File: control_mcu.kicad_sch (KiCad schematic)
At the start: 18 parts, among them J601 Conn_02x07_Counter_Clockwise, J602 Conn_01x02, U601 ATtiny1614-SSNR, U602 RCLAMP0524P-N

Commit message: SH-RPi v2 schematic design
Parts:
- removed D602, D603: MSK4005, Diode_SMD:D_SOD-523, symbol Device:D_Schottky
- removed J601: Conn_02x07_Counter_Clockwise, SH-RPi:PinHeader_2x07_P2.54mm_Vertical_CounterClockwise, symbol Connector_Generic:Conn_02x07_Counter_Clockwise
- removed U601: ATtiny1614-SSNR, Package_SO:SOIC-14_3.9x8.7mm_P1.27mm, symbol MCU_Microchip_ATtiny:ATtiny1614-SS
- removed U602: RCLAMP0524P-N, Package_DFN_QFN:Diodes_UDFN-10_1.0x2.5mm_P0.5mm, symbol SH-RPi:RCLAMP0524P-N
- added C402: 33pF/50V, Capacitor_SMD:C_0603_1608Metric, symbol Device:C
- added C405: 33pF, Capacitor_SMD:C_0402_1005Metric, symbol Device:C
- added D401, D402: ESD5451N, Diode_SMD:D_0402_1005Metric, symbol Device:D_TVS
- added FB402: GZ2012D101TF, Inductor_SMD:L_0805_2012Metric, symbol Device:FerriteBead
- added J402: Conn_01x02, Connector_PinHeader_2.54mm:PinHeader_1x02_P2.54mm_Vertical, symbol Connector_Generic:Conn_01x02
- added J403: Conn_02x06_Odd_Even, symbol Connector_Generic:Conn_02x06_Odd_Even
- added R406: 100R, Resistor_SMD:R_0603_1608Metric, symbol Device:R
- added R408: 1k, symbol Device:R_Small
- added R409: 10k, Resistor_SMD:R_0402_1005Metric, symbol Device:R
- added R410: 100k, Resistor_SMD:R_0402_1005Metric, symbol Device:R
- added U401: ATtiny1616-M, Package_DFN_QFN:VQFN-20-1EP_3x3mm_P0.4mm_EP1.7x1.7mm, symbol MCU_Microchip_ATtiny:ATtiny1616-M
- R402: renamed from R604; value 300k -> 150k; LCSC C25774 -> (none)
- R403: renamed from R605; value 200k -> 20k; LCSC C25764 -> (none)
- renumbered C603 to C401, C601 to C403, C604 to C404, C602 to C406, D601 to D403, FB601 to FB401, J602 to J401, R601 to R401, R602 to R404, R606 to R405, R603 to R407
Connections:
- net ATT_Vcc is gone; now on net +3V3: C406.1, D403.1 (K), R407.1
- net +3V3: now also J403.6 (Pin_6), U401.4 (VCC)
- net EN5V: now also R409.2, R410.1
- net GND: now also C402.2, C405.2, D401.1 (A1), D402.1 (A1), J402.2 (Pin_2), J403.7 (Pin_7), J403.8 (Pin_8), R410.2, U401.21 (GND), U401.3 (GND)
- net RESET: now also J403.3 (Pin_3), R408.2, U401.19 (~{RESET}/PA0)
- net RXD: now also J403.9 (Pin_9), U401.11 (PB3)
- net SCL: now also U401.14 (PB0)
- net SDA: now also U401.13 (PB1)
- net TXD: now also J403.11 (Pin_11), U401.12 (PB2)
- net VcapS: now also U401.8 (PA7)
- net VinS: now also U401.7 (PA6)
- net EXT_INT renamed EXT
- net EXT: now also U401.16 (PC1)
- net PB0_CONN renamed EXT_CONN
- net EXT_CONN: now also D401.2 (A2)
- new net: J403.1 (Pin_1), R408.1
- new net: C405.1, FB402.1, R406.2
- new net EN5V_MCU: R409.1, U401.18 (PC3)
- new net EN_OUT: J403.5 (Pin_5)
- new net Iin: U401.10 (PB4)
- new net LED_1: U401.1 (PA2)
- new net LED_2: U401.2 (PA3)
- new net LED_3: U401.5 (PA4)
- new net LED_4: U401.6 (PA5)
- new net POWER_TOGGLE: R406.1, U401.15 (PC0)
- new net POW_CONN: C402.1, D402.2 (A2), FB402.2, J402.1 (Pin_1)
- new net RTC_INT: U401.17 (PC2)
- new net RXD0: J403.12 (Pin_12)
- new net RXD5: J403.4 (Pin_4)
- new net TXD0: J403.10 (Pin_10)
- new net TXD5: J403.2 (Pin_2)
- no-connect marks 4 -> 2
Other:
- note added: "5V output enable interface"
- note added: "Clamp VinS to always less than 3V3"
- note added: "ESD and EMI protection for external connectors"
- note added: "Programming connector"
- note added: "Resistor pulls EN down when the MCU is unpowered"
- note added: "Scale Vcap down to ADC input"
- note added: "Scale Vin down to ADC input"
- note added: "VcapS is scaled from 9.35V to 1.1V (this will also drain the cap over time)"
- note removed: "Clamp VinS to always less than ATT_Vcc"
- note removed: "VcapS is scaled from 2.75V to 1.1V (this will also drain the cap over time)"
- moved on the sheet: C401, C403, C404, C406, D403, FB401, J401, R401, R402, R403, R404, R405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

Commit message: WIP: Assign footprints and LCSC part numbers
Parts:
- J403: footprint (none) -> Connector_PinHeader_2.54mm:PinHeader_2x06_P2.54mm_Vertical; LCSC (none) -> C492423
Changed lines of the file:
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@@
     (property "Reference" "J403" (id 0) (at 245.11 63.5 0))
     (property "Value" "Conn_02x06_Odd_Even" (id 1) (at 245.11 66.04 0))
-    (property "Footprint" "" (id 2) (at 243.84 74.93 0)
+    (property "Footprint" "Connector_PinHeader_2.54mm:PinHeader_2x06_P2.54mm_Vertical" (id 2) (at 243.84 74.93 0)
       (effects (font (size 1.27 1.27)) hide)
     )
@@
       (effects (font (size 1.27 1.27)) hide)
     )
+    (property "LCSC" "C492423" (id 4) (at 243.84 74.93 0)
+      (effects (font (size 1.27 1.27)) hide)
+    )

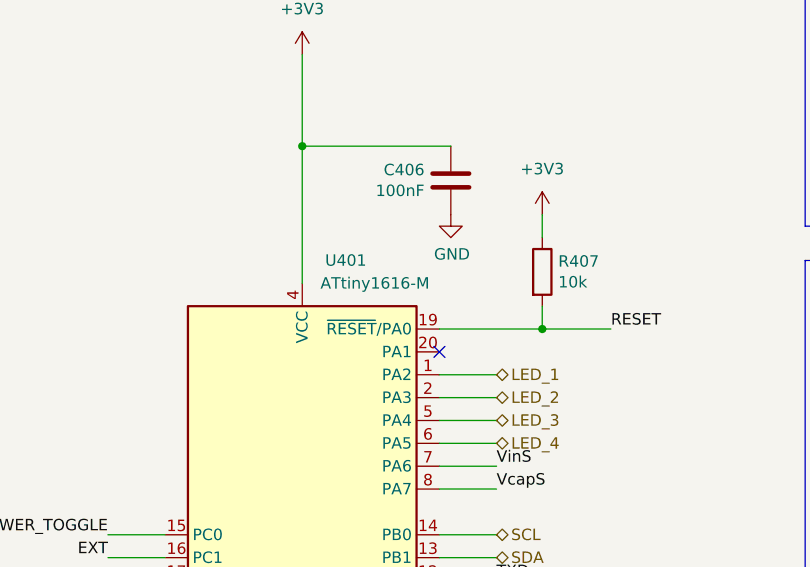
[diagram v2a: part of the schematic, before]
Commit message: Assign footprints and part numbers to components
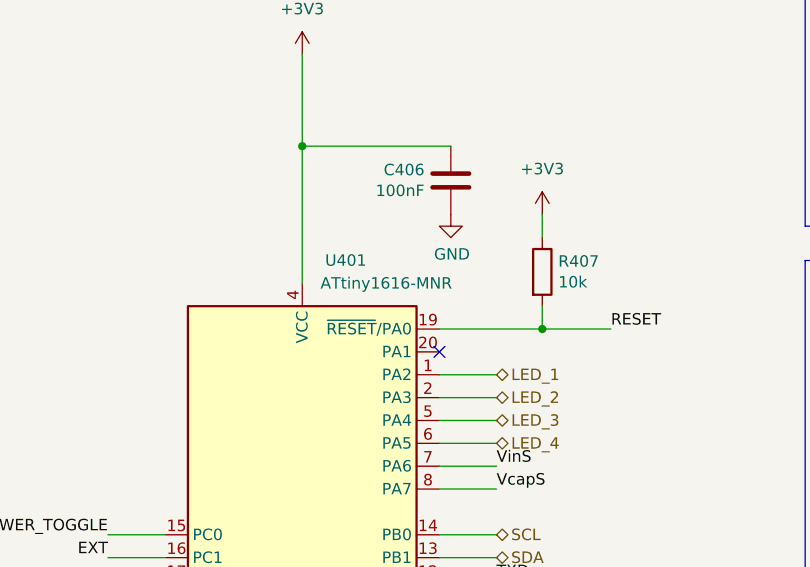
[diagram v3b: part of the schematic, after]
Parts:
- R402: LCSC (none) -> C25755
- R403: LCSC (none) -> C25765
- R408: footprint (none) -> Resistor_SMD:R_0402_1005Metric; LCSC (none) -> C11702
- U401: value ATtiny1616-M -> ATtiny1616-MNR; LCSC (none) -> C507118
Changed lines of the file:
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@@
       (effects (font (size 1.27 1.27)) hide)
     )
-    (property "LCSC" "" (id 4) (at 71.12 176.53 0)
+    (property "LCSC" "C25765" (id 4) (at 71.12 176.53 0)
       (effects (font (size 1.27 1.27)) hide)
     )
@@
       (effects (font (size 1.27 1.27)) hide)
     )
-    (property "LCSC" "" (id 4) (at 71.12 163.83 0)
+    (property "LCSC" "C25755" (id 4) (at 71.12 163.83 0)
       (effects (font (size 1.27 1.27)) hide)
     )
@@
       (effects (font (size 1.27 1.27)) (justify left))
     )
-    (property "Footprint" "" (id 2) (at 217.17 71.12 0)
+    (property "Footprint" "Resistor_SMD:R_0402_1005Metric" (id 2) (at 217.17 71.12 0)
       (effects (font (size 1.27 1.27)) hide)
     )
@@
       (effects (font (size 1.27 1.27)) hide)
     )
+    (property "LCSC" "C11702" (id 4) (at 217.17 71.12 0)
+      (effects (font (size 1.27 1.27)) hide)
+    )
     (pin "1")
     (pin "2")
@@
       (effects (font (size 1.27 1.27)) (justify left))
     )
-    (property "Value" "ATtiny1616-M" (id 1) (at 150.6094 55.88 0)
+    (property "Value" "ATtiny1616-MNR" (id 1) (at 150.6094 55.88 0)
       (effects (font (size 1.27 1.27)) (justify left))
     )
@@
       (effects (font (size 1.27 1.27)) hide)
     )
+    (property "LCSC" "C507118" (id 4) (at 148.59 78.74 0)
+      (effects (font (size 1.27 1.27)) hide)
+    )

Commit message: WIP: PCB layout
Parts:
- removed J401, J402: Conn_01x02, Connector_PinHeader_2.54mm:PinHeader_1x02_P2.54mm_Vertical, symbol Connector_Generic:Conn_01x02
- added J401: Conn_02x02_Top_Bottom, Connector_PinHeader_2.54mm:PinHeader_2x02_P2.54mm_Vertical, symbol Connector_Generic:Conn_02x02_Top_Bottom
- R401: value 62k -> 56k; footprint Resistor_SMD:R_0603_1608Metric -> Resistor_SMD:R_0402_1005Metric; LCSC C23221 -> C25796
- R404: value 2.2k -> 2k; LCSC C25879 -> C4109
- R405, R406: footprint Resistor_SMD:R_0603_1608Metric -> Resistor_SMD:R_0402_1005Metric; LCSC C22775 -> C25076
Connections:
- net EXT_CONN: now also J401.4 (Pin_4)
- net GND: now also J401.1 (Pin_1), J401.3 (Pin_3)
- net POW_CONN: now also J401.2 (Pin_2)
- net TXD5J: now reaches J403.1 (Pin_1), R408.1
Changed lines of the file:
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@@
     (stroke (width 0) (type default) (color 0 0 0 0))
   )
-  (wire (pts (xy 26.67 33.02) (xy 31.75 33.02))
+  (wire (pts (xy 19.05 33.02) (xy 31.75 33.02))
     (stroke (width 0) (type default) (color 0 0 0 0))
   )
@@
     (stroke (width 0) (type default) (color 0 0 0 0))
   )
-  (wire (pts (xy 26.67 30.48) (xy 39.37 30.48))
+  (wire (pts (xy 21.59 30.48) (xy 39.37 30.48))
     (stroke (width 0) (type default) (color 0 0 0 0))
   )
@@
     (stroke (width 0) (type default) (color 0 0 0 0))
   )
+  (wire (pts (xy 19.05 33.02) (xy 19.05 40.64))
+    (stroke (width 0) (type default) (color 0 0 0 0))
+  )
   (wire (pts (xy 163.83 76.2) (xy 170.18 76.2))
     (stroke (width 0) (type default) (color 0 0 0 0))
@@
     (stroke (width 0) (type default) (color 0 0 0 0))
   )
+  (wire (pts (xy 19.05 63.5) (xy 19.05 53.34))
+    (stroke (width 0) (type default) (color 0 0 0 0))
+  )
   (wire (pts (xy 251.46 74.93) (xy 262.89 74.93))
     (stroke (width 0) (type default) (color 0 0 0 0))
@@
     (stroke (width 0) (type default) (color 0 0 0 0))
   )
+  (wire (pts (xy 21.59 30.48) (xy 21.59 40.64))
+    (stroke (width 0) (type default) (color 0 0 0 0))
+  )
   (wire (pts (xy 41.91 118.11) (xy 64.77 118.11))
     (stroke (width 0) (type default) (color 0 0 0 0))
@@
     (stroke (width 0) (type default) (color 0 0 0 0))
   )
-  (wire (pts (xy 26.67 60.96) (xy 39.37 60.96))
+  (wire (pts (xy 21.59 60.96) (xy 39.37 60.96))
     (stroke (width 0) (type default) (color 0 0 0 0))
   )
@@
     (stroke (width 0) (type default) (color 0 0 0 0))
   )
+  (wire (pts (xy 21.59 60.96) (xy 21.59 53.34))
+    (stroke (width 0) (type default) (color 0 0 0 0))
+  )
   (polyline (pts (xy 269.24 53.34) (xy 269.24 87.63))
     (stroke (width 0) (type default) (color 0 0 0 0))
@@
     (stroke (width 0) (type default) (color 0 0 0 0))
   )
-  (wire (pts (xy 26.67 63.5) (xy 31.75 63.5))
+  (wire (pts (xy 19.05 63.5) (xy 31.75 63.5))
     (stroke (width 0) (type default) (color 0 0 0 0))
   )
@@
     (effects (font (size 1.27 1.27)) (justify right bottom))
   )
+  (label "TXD5J" (at 236.22 69.85 180)
+    (effects (font (size 1.27 1.27)) (justify right bottom))
+  )
   (label "POW_CONN" (at 44.45 60.96 0)
     (effects (font (size 1.27 1.27)) (justify left bottom))
@@
       (effects (font (size 1.27 1.27)) (justify left))
     )
-    (property "Value" "62k" (id 1) (at 66.548 112.903 0)
-      (effects (font (size 1.27 1.27)) (justify left))
-    )
-    (property "Footprint" "Resistor_SMD:R_0603_1608Metric" (id 2) (at 62.992 111.76 90)
+    (property "Value" "56k" (id 1) (at 66.548 112.903 0)
+      (effects (font (size 1.27 1.27)) (justify left))
+    )
+    (property "Footprint" "Resistor_SMD:R_0402_1005Metric" (id 2) (at 62.992 111.76 90)
       (effects (font (size 1.27 1.27)) hide)
     )
@@
       (effects (font (size 1.27 1.27)) hide)
     )
-    (property "LCSC" "C23221" (id 4) (at 64.77 111.76 0)
+    (property "LCSC" "C25796" (id 4) (at 64.77 111.76 0)
       (effects (font (size 1.27 1.27)) hide)
     )
@@
       (effects (font (size 1.27 1.27)) (justify left))
     )
-    (property "Value" "2.2k" (id 1) (at 81.788 125.603 0)
+    (property "Value" "2k" (id 1) (at 81.788 125.603 0)
       (effects (font (size 1.27 1.27)) (justify left))
     )
@@
       (effects (font (size 1.27 1.27)) hide)
     )
-    (property "LCSC" "C25879" (id 4) (at 80.01 124.46 0)
+    (property "LCSC" "C4109" (id 4) (at 80.01 124.46 0)
       (effects (font (size 1.27 1.27)) hide)
     )
@@
     )
     (property "LCSC" "C25755" (id 4) (at 71.12 163.83 0)
-      (effects (font (size 1.27 1.27)) hide)
-    )
-    (pin "1")
-    (pin "2")
-  )
-  (symbol (lib_id "Connector_Generic:Conn_01x02") (at 21.59 30.48 0) (mirror y) (unit 1)
-    (in_bom yes) (on_board yes)
-    (property "Reference" "J401" (id 0) (at 23.6728 24.9682 0))
-    (property "Value" "Conn_01x02" (id 1) (at 23.6728 27.2796 0))
-    (property "Footprint" "Connector_PinHeader_2.54mm:PinHeader_1x02_P2.54mm_Vertical" (id 2) (at 21.59 30.48 0)
-      (effects (font (size 1.27 1.27)) hide)
-    )
-    (property "Datasheet" "~" (id 3) (at 21.59 30.48 0)
-      (effects (font (size 1.27 1.27)) hide)
-    )
-    (property "LCSC" "C492401" (id 4) (at 21.59 30.48 0)
       (effects (font (size 1.27 1.27)) hide)
     )
@@
     (property "Reference" "R405" (id 0) (at 81.28 25.2222 90))
     (property "Value" "100R" (id 1) (at 81.28 27.5336 90))
-    (property "Footprint" "Resistor_SMD:R_0603_1608Metric" (id 2) (at 81.28 28.702 90)
+    (property "Footprint" "Resistor_SMD:R_0402_1005Metric" (id 2) (at 81.28 28.702 90)
       (effects (font (size 1.27 1.27)) hide)
     )
@@
       (effects (font (size 1.27 1.27)) hide)
     )
-    (property "LCSC" "C22775" (id 4) (at 81.28 30.48 90)
+    (property "LCSC" "C25076" (id 4) (at 81.28 30.48 90)
       (effects (font (size 1.27 1.27)) hide)
     )
@@
     (property "Reference" "R406" (id 0) (at 81.28 55.7022 90))
     (property "Value" "100R" (id 1) (at 81.28 58.0136 90))
-    (property "Footprint" "Resistor_SMD:R_0603_1608Metric" (id 2) (at 81.28 59.182 90)
+    (property "Footprint" "Resistor_SMD:R_0402_1005Metric" (id 2) (at 81.28 59.182 90)
       (effects (font (size 1.27 1.27)) hide)
     )
@@
       (effects (font (size 1.27 1.27)) hide)
     )
-    (property "LCSC" "C22775" (id 4) (at 81.28 60.96 90)
-      (effects (font (size 1.27 1.27)) hide)
-    )
-    (pin "1")
-    (pin "2")
-  )
-  (symbol (lib_id "Connector_Generic:Conn_01x02") (at 21.59 60.96 0) (mirror y) (unit 1)
-    (in_bom yes) (on_board yes)
-    (property "Reference" "J402" (id 0) (at 23.6728 55.4482 0))
-    (property "Value" "Conn_01x02" (id 1) (at 23.6728 57.7596 0))
-    (property "Footprint" "Connector_PinHeader_2.54mm:PinHeader_1x02_P2.54mm_Vertical" (id 2) (at 21.59 60.96 0)
-      (effects (font (size 1.27 1.27)) hide)
-    )
-    (property "Datasheet" "~" (id 3) (at 21.59 60.96 0)
-      (effects (font (size 1.27 1.27)) hide)
-    )
-    (property "LCSC" "C492401" (id 4) (at 21.59 60.96 0)
+    (property "LCSC" "C25076" (id 4) (at 81.28 60.96 90)
       (effects (font (size 1.27 1.27)) hide)
     )
@@
     (pin "1")
   )
+  (symbol (lib_id "Connector_Generic:Conn_02x02_Top_Bottom") (at 19.05 48.26 90) (unit 1)
+    (in_bom yes) (on_board yes)
+    (property "Reference" "J401" (id 0) (at 22.86 52.07 90)
+      (effects (font (size 1.27 1.27)) (justify right))
+    )
+    (property "Value" "Conn_02x02_Top_Bottom" (id 1) (at 22.86 54.61 90)
+      (effects (font (size 1.27 1.27)) (justify right))
+    )
+    (property "Footprint" "Connector_PinHeader_2.54mm:PinHeader_2x02_P2.54mm_Vertical" (id 2) (at 19.05 48.26 0)
+      (effects (font (size 1.27 1.27)) hide)
+    )
+    (property "Datasheet" "~" (id 3) (at 19.05 48.26 0)
+      (effects (font (size 1.27 1.27)) hide)
+    )
+    (pin "1")
+    (pin "2")
+    (pin "3")
+    (pin "4")
+  )
 )

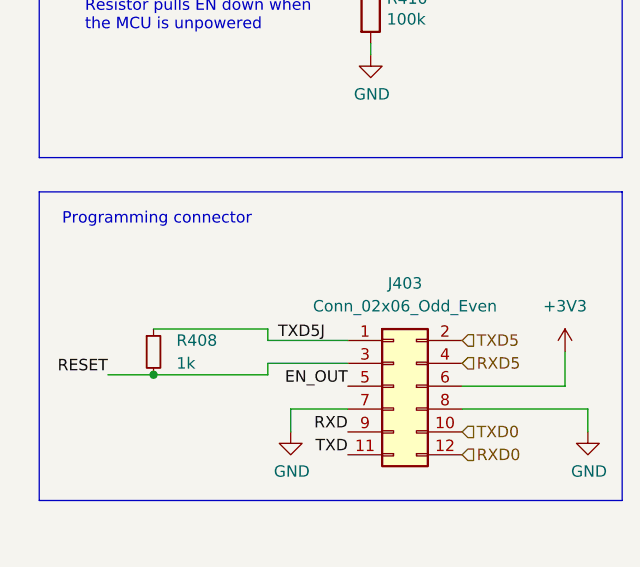
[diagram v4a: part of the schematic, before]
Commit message: Initial PCB component layout done
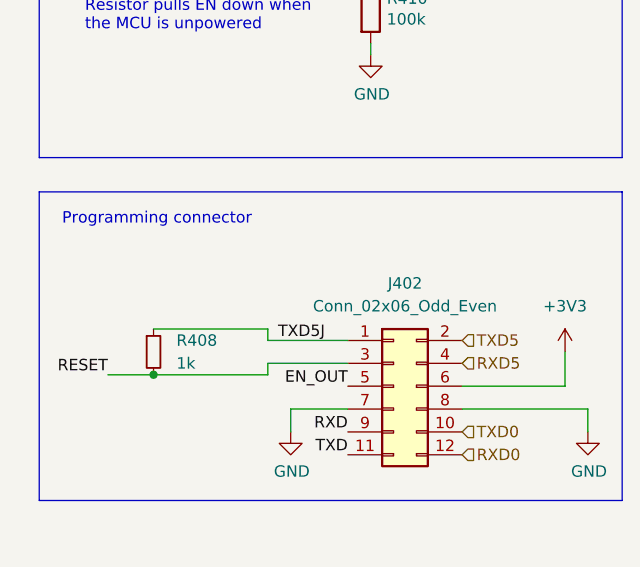
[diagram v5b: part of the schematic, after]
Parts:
- renumbered J403 to J402
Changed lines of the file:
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@@
   (symbol (lib_id "Connector_Generic:Conn_02x06_Odd_Even") (at 243.84 74.93 0) (unit 1)
     (in_bom yes) (on_board yes) (fields_autoplaced)
-    (property "Reference" "J403" (id 0) (at 245.11 63.5 0))
+    (property "Reference" "J402" (id 0) (at 245.11 63.5 0))
     (property "Value" "Conn_02x06_Odd_Even" (id 1) (at 245.11 66.04 0))
     (property "Footprint" "Connector_PinHeader_2.54mm:PinHeader_2x06_P2.54mm_Vertical" (id 2) (at 243.84 74.93 0)

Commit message: Finish PCB routing
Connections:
- net EN_OUT is gone; now on net EN5V: J402.5 (Pin_5)
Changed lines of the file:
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@@
     (effects (font (size 1.27 1.27)) (justify left bottom))
   )
-  (label "EN_OUT" (at 238.76 74.93 180)
+  (label "EN5V" (at 238.76 74.93 180)
     (effects (font (size 1.27 1.27)) (justify right bottom))
   )

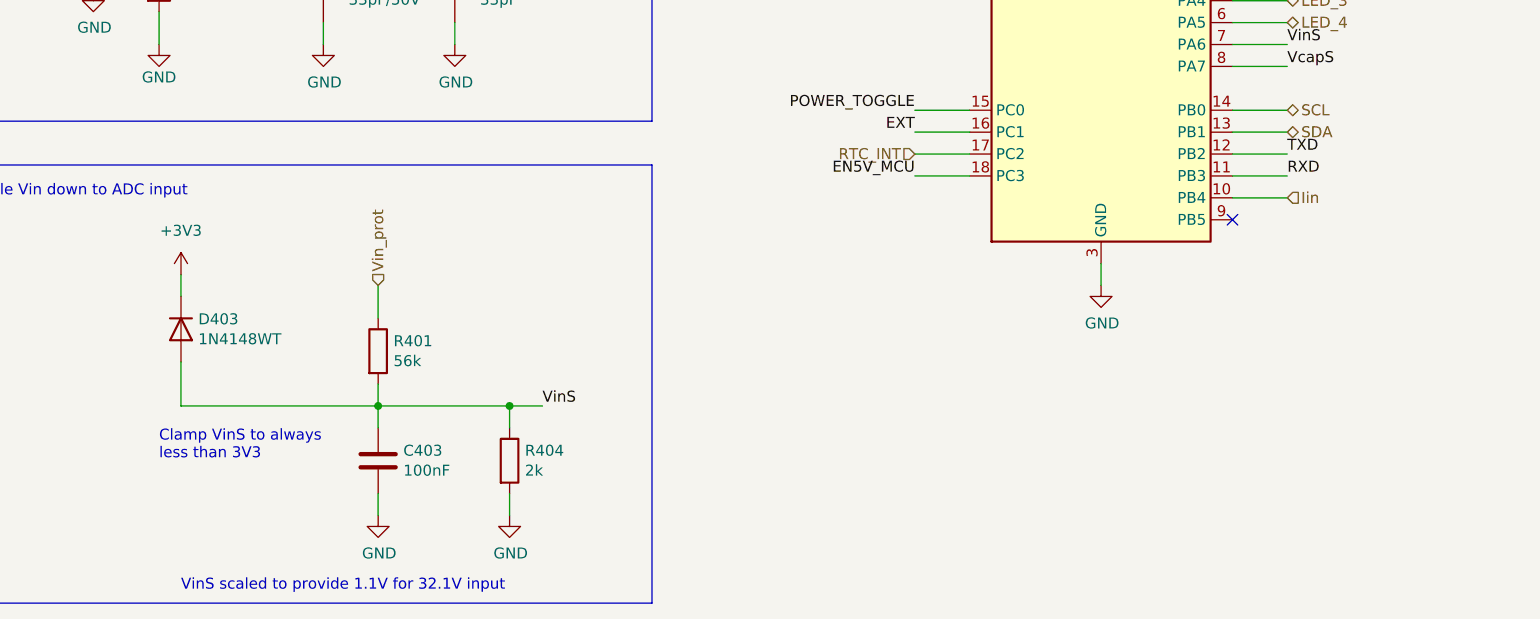
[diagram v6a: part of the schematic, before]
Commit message: Replace "ideal diode" with Schottky & other changes
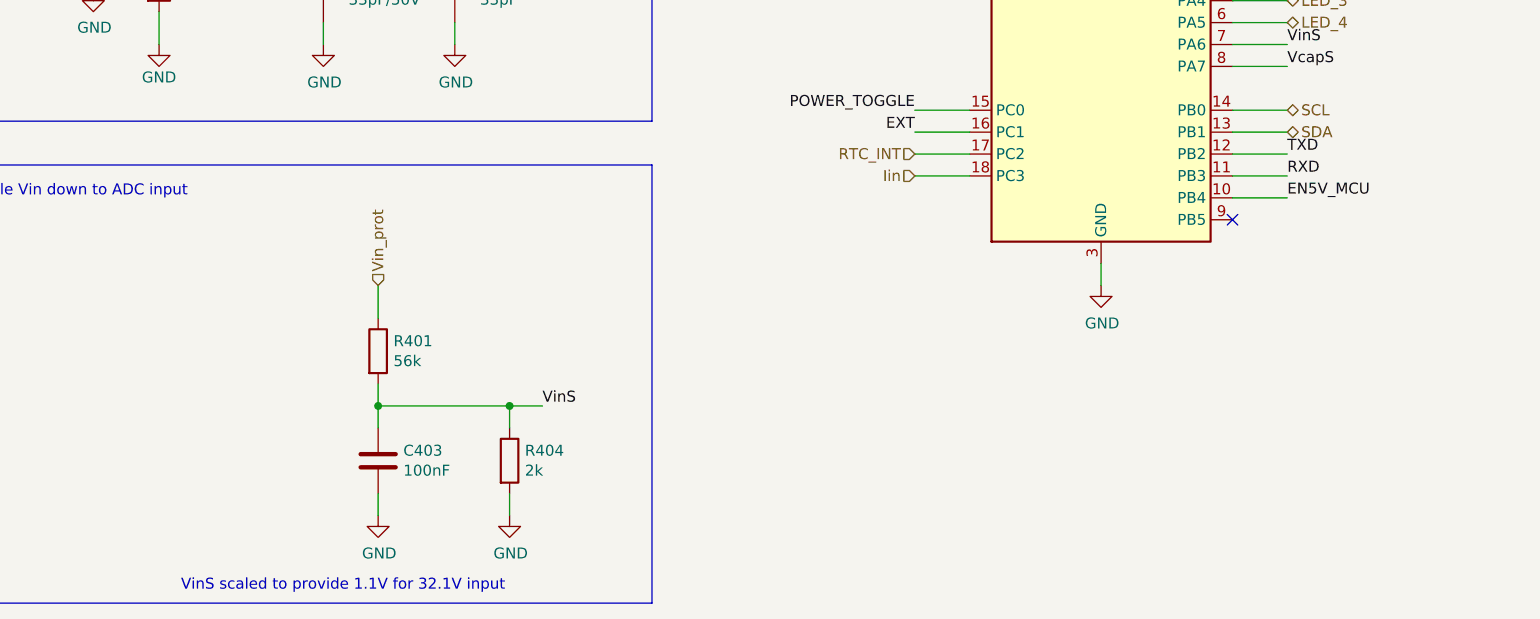
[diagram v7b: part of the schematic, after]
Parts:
- removed D403: 1N4148WT, Diode_SMD:D_SOD-523, symbol Device:D
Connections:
- net EN5V_MCU: now also U401.10 (PB4); no longer U401.18 (PC3)
- net Iin: now also U401.18 (PC3); no longer U401.10 (PB4)
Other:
- note removed: "Clamp VinS to always less than 3V3"
